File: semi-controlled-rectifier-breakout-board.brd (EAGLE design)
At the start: 118.1 x 165.1 mm, 18 parts, among them U10 VO3053-X007T, U11 VO3053-X007T, U8 TN4015H-6G, U9 TN4015H-6G, X1 22-23-2031

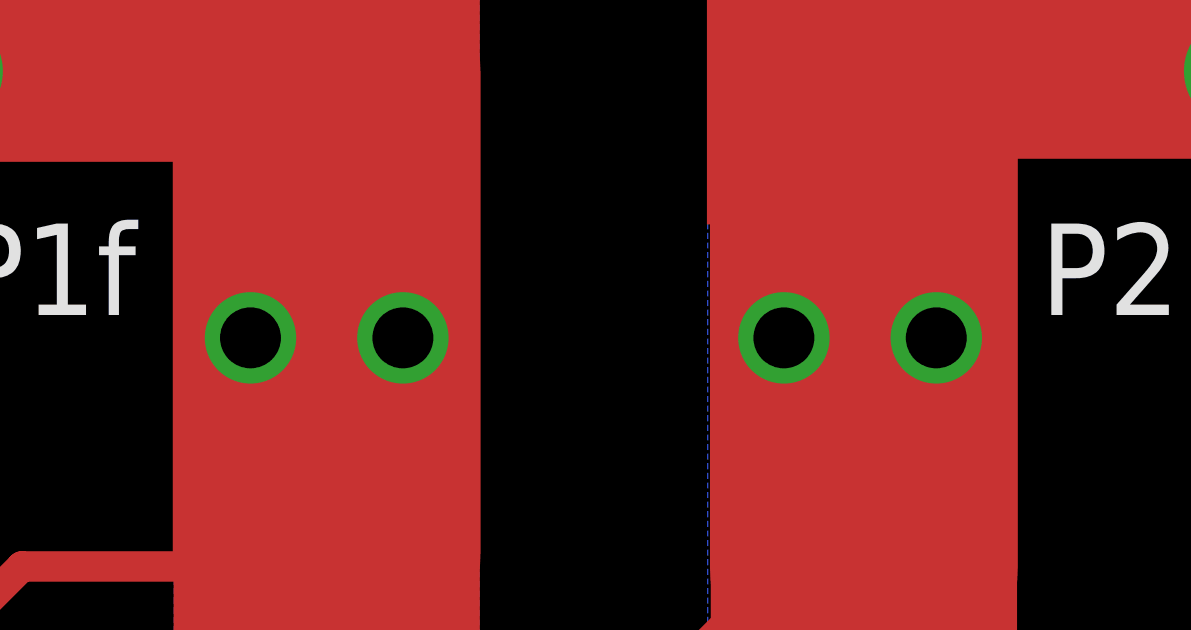
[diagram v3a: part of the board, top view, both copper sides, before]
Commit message: Added extra vias and updated flatcam project
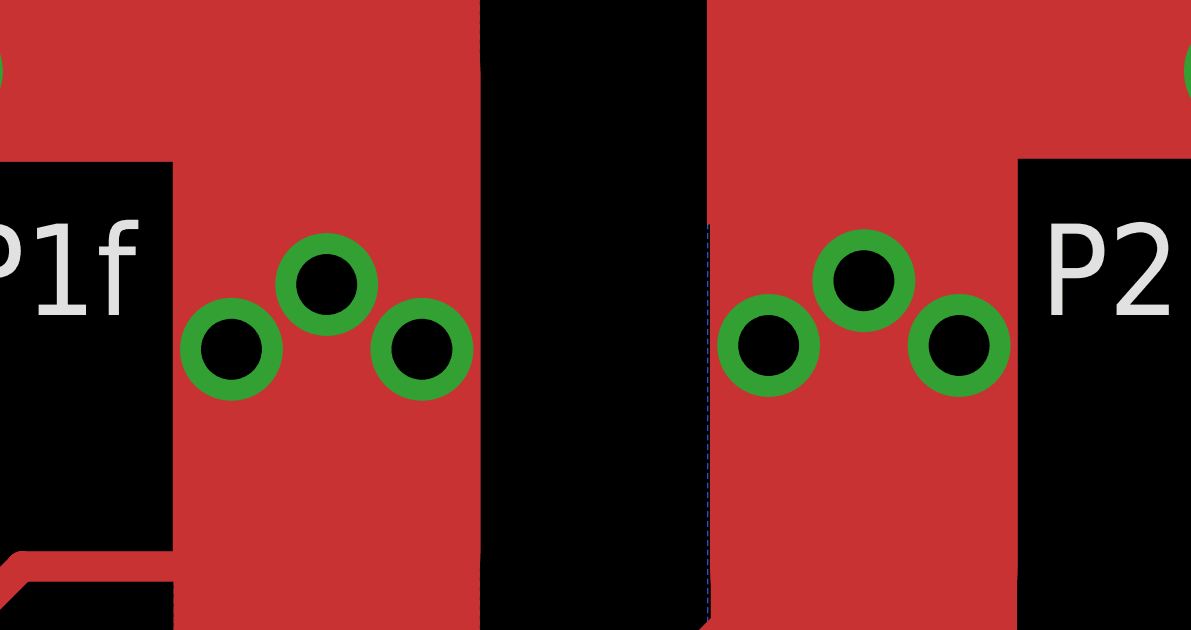
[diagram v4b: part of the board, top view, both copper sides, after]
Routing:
- net P2_IN: vias 2 -> 3
- net P1_FUSED: vias 2 -> 3
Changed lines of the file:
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@@
 <vertex x="38.1" y="106.68"/>
 </polygon>
-<via x="40.64" y="119.38" extent="1-16" drill="2.032"/>
-<via x="45.72" y="119.38" extent="1-16" drill="2.032"/>
-<wire x1="45.72" y1="119.38" x2="43.307" y2="111.7346" width="0" layer="19" extent="1-1"/>
+<via x="46.482" y="119.126" extent="1-16" drill="2.032" diameter="3.429"/>
+<via x="40.132" y="119.126" extent="1-16" drill="2.032" diameter="3.429"/>
+<via x="43.307" y="121.285" extent="1-16" drill="2.032" diameter="3.429"/>
+<wire x1="43.307" y1="121.285" x2="43.18" y2="128.1684" width="0" layer="19" extent="1-1"/>
 </signal>
 <signal name="P1_FUSED">
@@
 <vertex x="20.32" y="106.68"/>
 </polygon>
-<via x="27.94" y="119.38" extent="1-16" drill="2.032"/>
-<via x="22.86" y="119.38" extent="1-16" drill="2.032"/>
+<via x="28.575" y="118.999" extent="1-16" drill="2.032" diameter="3.429"/>
+<via x="22.225" y="118.999" extent="1-16" drill="2.032" diameter="3.429"/>
+<via x="25.4" y="121.158" extent="1-16" drill="2.032" diameter="3.429"/>
 <wire x1="25.4" y1="111.8616" x2="25.4" y2="112.268" width="0" layer="19" extent="1-1"/>
-<wire x1="22.86" y1="119.38" x2="25.4" y2="112.268" width="0" layer="19" extent="1-1"/>
+<wire x1="25.4" y1="121.158" x2="25.4" y2="128.1684" width="0" layer="19" extent="1-1"/>
 </signal>
 <signal name="DC+">
